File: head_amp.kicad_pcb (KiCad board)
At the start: 4 copper layers, 50 x 50 mm, 66 parts, among them J1 USB Interface, J2 Left_Speaker, J3 Left_Mic, J4 Right_Speaker, J5 Right_Mic, J6 AudioJack4, M1 Fan, Q1 LRC L8050QLT1G, Q2 LRC L8050QLT1G, SW1 Boot, SW2 Reset, U1 CH340K, U2 Digital Regulator, U3 Analog Regulator, U4 TXS0102DCU, U5 ESP32-S3-WROOM-1, U6 LSM6DS3, U7 WM8988LGECN/V, U8 WM8988LGECN/V

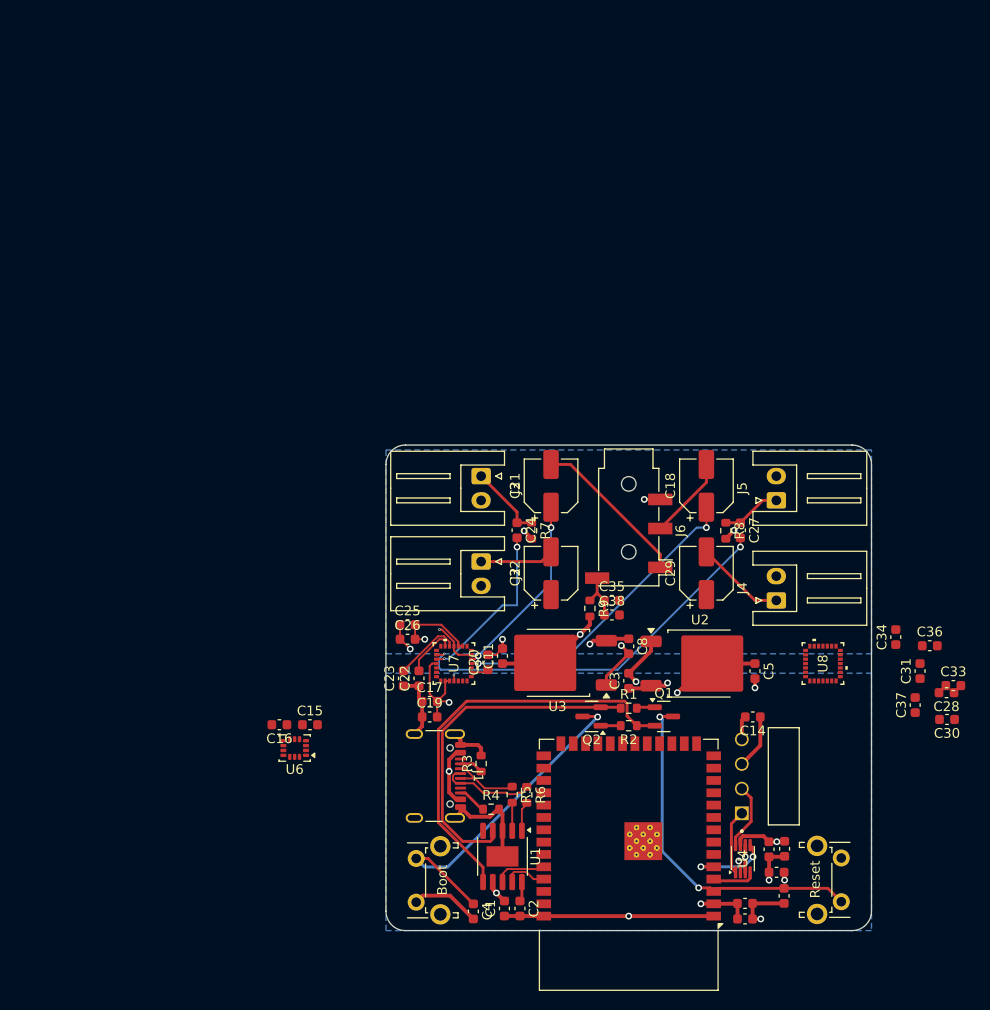
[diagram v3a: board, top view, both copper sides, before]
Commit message: feat: start hat version
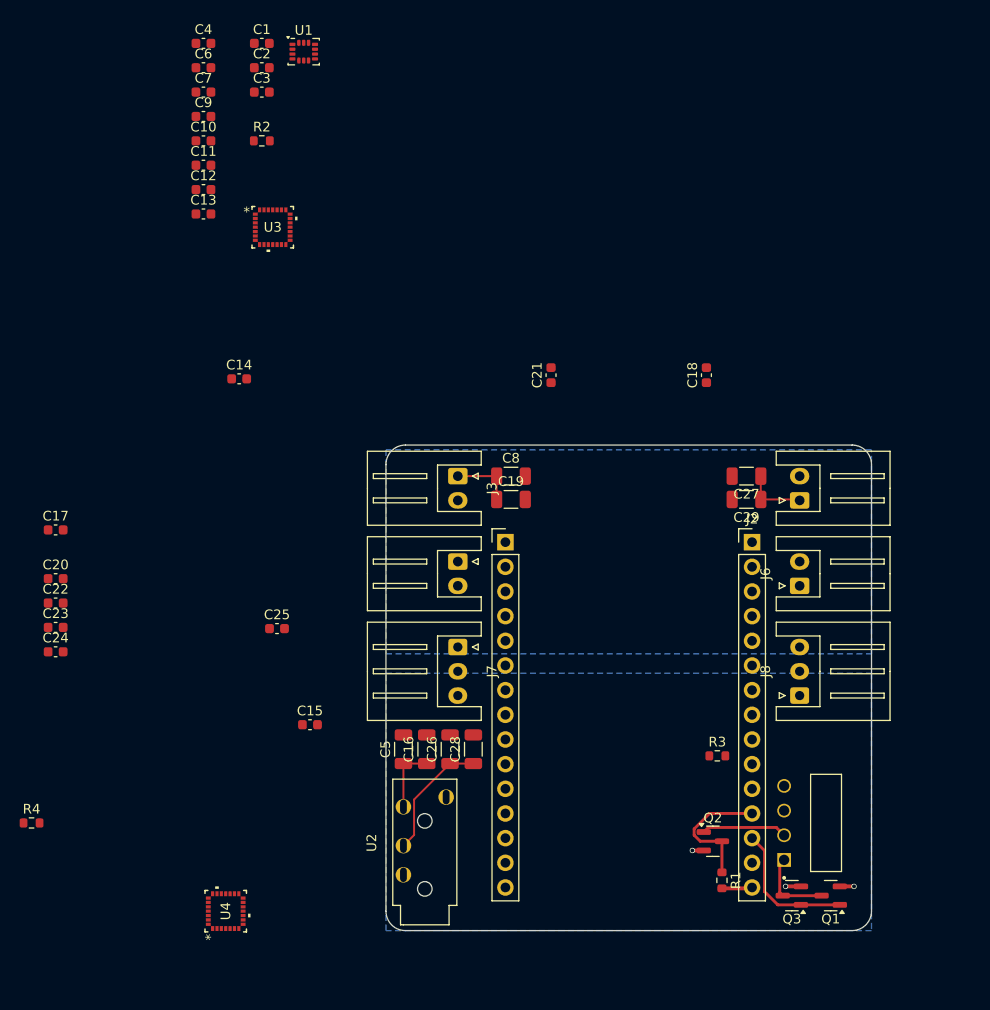
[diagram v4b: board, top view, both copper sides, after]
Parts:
- removed C30: 100n, Capacitor_SMD:C_0603_1608Metric
- removed C31, C33, C34, C36, C37: 4.7u, Capacitor_SMD:C_0603_1608Metric
- removed C32: 220u, Capacitor_SMD:CP_Elec_5x5.4
- removed C35, C38: 1u, Capacitor_SMD:C_0603_1608Metric
- removed R5, R6: 22, Resistor_SMD:R_0603_1608Metric
- removed R7, R8, R9: 10k, Resistor_SMD:R_0603_1608Metric
- removed SW1: Boot, Button_Switch_THT:SW_Tactile_SPST_Angled_PTS645Vx39-2LFS
- removed SW2: Reset, Button_Switch_THT:SW_Tactile_SPST_Angled_PTS645Vx39-2LFS
- removed U5: ESP32-S3-WROOM-1, RF_Module:ESP32-S3-WROOM-1
- removed U6: LSM6DS3, Package_LGA:LGA-14_3x2.5mm_P0.5mm_LayoutBorder3x4y
- removed U7, U8: WM8988LGECN/V, footprints:QFN28_4X4_CIR-M
- added J7: Conn_01x03, Connector_JST:JST_XH_S3B-XH-A_1x03_P2.50mm_Horizontal, F.Cu at (130.4, 96.8)
- added J8: Conn_01x03, Connector_JST:JST_XH_S3B-XH-A_1x03_P2.50mm_Horizontal, F.Cu at (165.6, 101.8)
- added Q3: AO3400A, Package_TO_SOT_SMD:SOT-23, F.Cu at (164.8, 122.4)
- C10, C12, C7: value 100n -> 4.7u
- C11: value 22u -> 1u
- C13, C24, C9: value 1u -> 4.7u
- C14: value 100n -> 1u
- C16, C19, C28: value 100n -> 100u; footprint Capacitor_SMD:C_0603_1608Metric -> Capacitor_SMD:C_1206_3216Metric
- C18, C21: value 220u -> 4.7u; footprint Capacitor_SMD:CP_Elec_5x5.4 -> Capacitor_SMD:C_0603_1608Metric
- C22, C25: value 4.7u -> 1u
- C26: value 4.7u -> 100u; footprint Capacitor_SMD:C_0603_1608Metric -> Capacitor_SMD:C_1206_3216Metric
- C27: value 1u -> 100u; footprint Capacitor_SMD:C_0603_1608Metric -> Capacitor_SMD:C_1206_3216Metric
- C29: value 220u -> 100u; footprint Capacitor_SMD:CP_Elec_5x5.4 -> Capacitor_SMD:C_1206_3216Metric
- C3: value 10u -> 100n
- C5: value 22u -> 100u; footprint Capacitor_SMD:C_0603_1608Metric -> Capacitor_SMD:C_1206_3216Metric
- C8: value 10u -> 100u; footprint Capacitor_SMD:C_0603_1608Metric -> Capacitor_SMD:C_1206_3216Metric
- J1: value USB Interface -> Conn_01x15; footprint Connector_USB:USB_C_Receptacle_GCT_USB4105-xx-A_16P_TopMnt_Horizontal -> Connector_PinHeader_2.54mm:PinHeader_1x15_P2.54mm_Vertical
- J2: value Left_Speaker -> Conn_01x15; footprint Connector_JST:JST_XH_S2B-XH-A_1x02_P2.50mm_Horizontal -> Connector_PinHeader_2.54mm:PinHeader_1x15_P2.54mm_Vertical
- J3: value Left_Mic -> Left_Speaker
- J4: value Right_Speaker -> Left_Mic
- J5: value Right_Mic -> Right_Speaker
- J6: value AudioJack4 -> Right_Mic; footprint Connector_Audio:Jack_3.5mm_PJ320D_Horizontal -> Connector_JST:JST_XH_S2B-XH-A_1x02_P2.50mm_Horizontal
- Q1: value LRC L8050QLT1G -> AO3401A
- Q2: value LRC L8050QLT1G -> AO3400A
- R3, R4: value 5.1k -> 10k
- U1: value CH340K -> LSM6DS3; footprint Package_SO:SSOP-10-1EP_3.9x4.9mm_P1mm_EP2.1x3.3mm -> Package_LGA:LGA-14_3x2.5mm_P0.5mm_LayoutBorder3x4y
- U2: value Digital Regulator -> PJ-320A; footprint Package_TO_SOT_SMD:TO-252-2 -> PJ-320A:PJ-320A
- U3: value Analog Regulator -> WM8988LGECN/V; footprint Package_TO_SOT_SMD:TO-252-2 -> footprints:QFN28_4X4_CIR-M
- U4: value TXS0102DCU -> WM8988LGECN/V; footprint Package_SO:VSSOP-8_2.3x2mm_P0.5mm -> footprints:QFN28_4X4_CIR-M
- moved C6 104.2 mm to (104.2, 37.1), turned to 0 degrees
- moved C7 99.7 mm to (104.2, 39.7)
- moved C9 98.4 mm to (104.2, 42.2), turned to 0 degrees
- moved C10 97.6 mm to (104.2, 44.7), turned to 0 degrees
- moved C4 93.6 mm to (104.2, 34.6), turned to 0 degrees
- moved C1 92.5 mm to (110.2, 34.6), turned to 0 degrees
- moved C2 90.6 mm to (110.2, 37.1), turned to 0 degrees
- moved C12 89.5 mm to (104.2, 49.7), turned to 0 degrees
- moved C13 88.6 mm to (104.2, 52.2), turned to 0 degrees
- moved U1 85.4 mm to (114.5, 35.5), turned to 0 degrees
- moved C3 71.4 mm to (110.2, 39.7), turned to 0 degrees
- moved R2 71.1 mm to (110.2, 44.7), turned to 0 degrees
- moved C14 63.3 mm to (107.9, 69.2), turned to 0 degrees
- moved C11 59.2 mm to (104.2, 47.2), turned to 0 degrees
- moved U3 53.6 mm to (111.3, 53.6), turned to 0 degrees
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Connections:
- C1 pad 1: GND -> +5V
- C1 pad 2: +3V3D -> GND
- C10 pad 2: +3V3D -> Net-(U3-VREF)
- C11 pad 1: +3V3A -> /Mic_Left
- C11 pad 2: GNDA -> Net-(U3-LINPUT1)
- C12 pad 1: GND -> GNDA
- C12 pad 2: VBUS -> +3V3A
- C13 pad 1: GND -> GNDA
- C13 pad 2: VBUS -> +3V3A
- C14 pad 1: VBUS -> /Mic_Right
- C14 pad 2: GND -> Net-(U3-RINPUT1)
- C15 pad 1: +3V3D -> GND
- C15 pad 2: GND -> +3V3D
- C16 pad 1: +3V3D -> /Headset_Left
- C16 pad 2: GND -> Net-(U3-LOUT1)
- C18 pad 1: Net-(U7-ROUT1) -> Net-(U4-HPCOM)
- C18 pad 2: /Headset_Right -> GNDA
- C19 pad 1: GND -> /Speaker_Left
- C19 pad 2: +3V3D -> Net-(U4-LOUT1)
- C2 pad 1: Net-(U1-V3) -> +3V3D
- C20 pad 1: Net-(U7-HPCOM) -> GND
- C20 pad 2: GNDA -> Net-(U4-VMID)
- C21 pad 1: Net-(U7-LOUT1) -> GND
- C21 pad 2: /Headset_Left -> Net-(U4-VREF)
- C22 pad 1: GND -> /Headset_Mic
- C22 pad 2: Net-(U7-VMID) -> Net-(U4-LINPUT1)
- C23 pad 1: GND -> GNDA
- C23 pad 2: Net-(U7-VREF) -> +3V3A
- C24 pad 1: /Mic_Left -> GNDA
- C24 pad 2: Net-(U7-LINPUT1) -> +3V3A
- C25 pad 1: GNDA -> /Headset_Mic
- C25 pad 2: +3V3A -> Net-(U4-RINPUT1)
- C26 pad 1: GNDA -> /Headset_Right
- C26 pad 2: +3V3A -> Net-(U3-ROUT1)
- C27 pad 1: /Mic_Right -> /Speaker_Right
- C27 pad 2: Net-(U7-RINPUT1) -> Net-(U4-ROUT1)
- C28 pad 1: GND -> /Headset_Right
- C28 pad 2: +3V3D -> Net-(U3-ROUT1)
- C29 pad 1: Net-(U8-ROUT1) -> /Speaker_Right
- C29 pad 2: /Speaker_Right -> Net-(U4-ROUT1)
- C3 pad 1: VBUS -> +3V3D
- C4 pad 1: /GPIO0 -> GND
- C4 pad 2: GND -> +3V3D
- C5 pad 1: +3V3D -> /Headset_Left
- C5 pad 2: GND -> Net-(U3-LOUT1)
- C6 pad 1: /MCU_EN -> GND
- C6 pad 2: GND -> +3V3D
- C7 pad 1: GND -> Net-(U3-HPCOM)
- C7 pad 2: +3V3D -> GNDA
- C8 pad 1: VBUS -> /Speaker_Left
- C8 pad 2: GNDA -> Net-(U4-LOUT1)
- C9 pad 2: +3V3D -> Net-(U3-VMID)
- J2 pad 1: /Speaker_Left -> unconnected-(J2-Pin_1-Pad1)
- J2 pad 2: GNDA -> unconnected-(J2-Pin_2-Pad2)
- J3 pad 1: /Mic_Left -> /Speaker_Left
- J4 pad 1: /Speaker_Right -> /Mic_Left
- J5 pad 1: /Mic_Right -> /Speaker_Right
- M1 pad 2: VBUS -> +5V
- Q1 pad 1: Net-(Q1-B) -> /FAN_PWM
- Q1 pad 2: /RTS -> +5V
- Q1 pad 3: /MCU_EN -> Net-(M1-PWM)
- Q2 pad 1: Net-(Q2-B) -> Net-(M1-Tacho)
- Q2 pad 2: /DTR -> GND
- Q2 pad 3: /GPIO0 -> /FAN_RPM
- R1 pad 1: /DTR -> /FAN_RPM
- R1 pad 2: Net-(Q1-B) -> +3V3D
- R2 pad 1: /RTS -> /Mic_Left
- R2 pad 2: Net-(Q2-B) -> +3V3A
- R3 pad 1: Net-(J1-CC1) -> /Mic_Right
- R3 pad 2: GND -> +3V3A
- R4 pad 1: Net-(J1-CC2) -> +3V3A
- R4 pad 2: GND -> /Headset_Mic
- U1 pad 1: /USB_D+ -> /MISO
- U1 pad 10: Net-(U1-V3) -> unconnected-(U1-NC-Pad10)
- U1 pad 11: GND -> unconnected-(U1-NC-Pad11)
- U1 pad 2: /USB_D- -> GND
- U1 pad 4: /DTR -> unconnected-(U1-INT1-Pad4)
- U1 pad 5: unconnected-(U1-~{CTS}-Pad5) -> +3V3D
- U1 pad 6: /RTS -> GND
- U1 pad 7: +3V3D -> GND
- U1 pad 8: /MCU_RX -> +3V3D
- U1 pad 9: /MCU_TX -> unconnected-(U1-INT2-Pad9)
- U2 pad 1: GND -> /Headset_Mic
- U2 pad 2: +3V3D -> /Headset_Left
- U2 pad 3: VBUS -> /Headset_Right
- U3 pad 1: GNDA -> /Ext->Int/Master_CLK
- U3 pad 2: +3V3A -> +3V3D
- U3 pad 3: VBUS -> +3V3D
- U4 pad 1: Net-(M1-PWM) -> /Int->Ext/Master_CLK
- U4 pad 2: GND -> +3V3D
- U4 pad 4: /FAN_PWM -> GND
- U4 pad 5: /FAN_RPM -> /Int->Ext_CLK
- U4 pad 6: +3V3D -> /Int->Ext_In
- U4 pad 7: VBUS -> /Int->Ext_LRC
- U4 pad 8: Net-(M1-Tacho) -> /Int->Ext_Out
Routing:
- net GND: track 72.5 -> 2.76 mm, vias 7 -> 2
- net /RTS: track 42.9 -> 0.00 mm
- net Net-(U7-RINPUT1): track 39.8 -> 0.00 mm, vias 2 -> 0
- net /MCU_EN: track 36.2 -> 0.00 mm, vias 2 -> 0
- net /DTR: track 35.7 -> 0.00 mm
- net /GPIO0: track 34.9 -> 0.00 mm, vias 1 -> 0
- net Net-(U7-ROUT1): track 32.1 -> 0.00 mm, vias 2 -> 0
- net +3V3D: track 31.2 -> 3.14 mm, vias 6 -> 0
- net VBUS: track 26.0 -> 0.00 mm, vias 4 -> 0
- net +3V3A: track 22.5 -> 0.00 mm, vias 4 -> 0
- net Net-(U7-LOUT1): track 19.3 -> 0.00 mm, vias 2 -> 0
- net GNDA: track 17.6 -> 0.00 mm, vias 5 -> 0
- net Net-(U7-LINPUT1): track 17.5 -> 0.00 mm, vias 2 -> 0
- net /FAN_PWM: track 4.55 -> 14.4 mm
- net /USB_D1+: track 9.79 -> 0.00 mm
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- added copper zone on In1.Cu, net +5V
- removed copper zone on In1.Cu, net VBUS

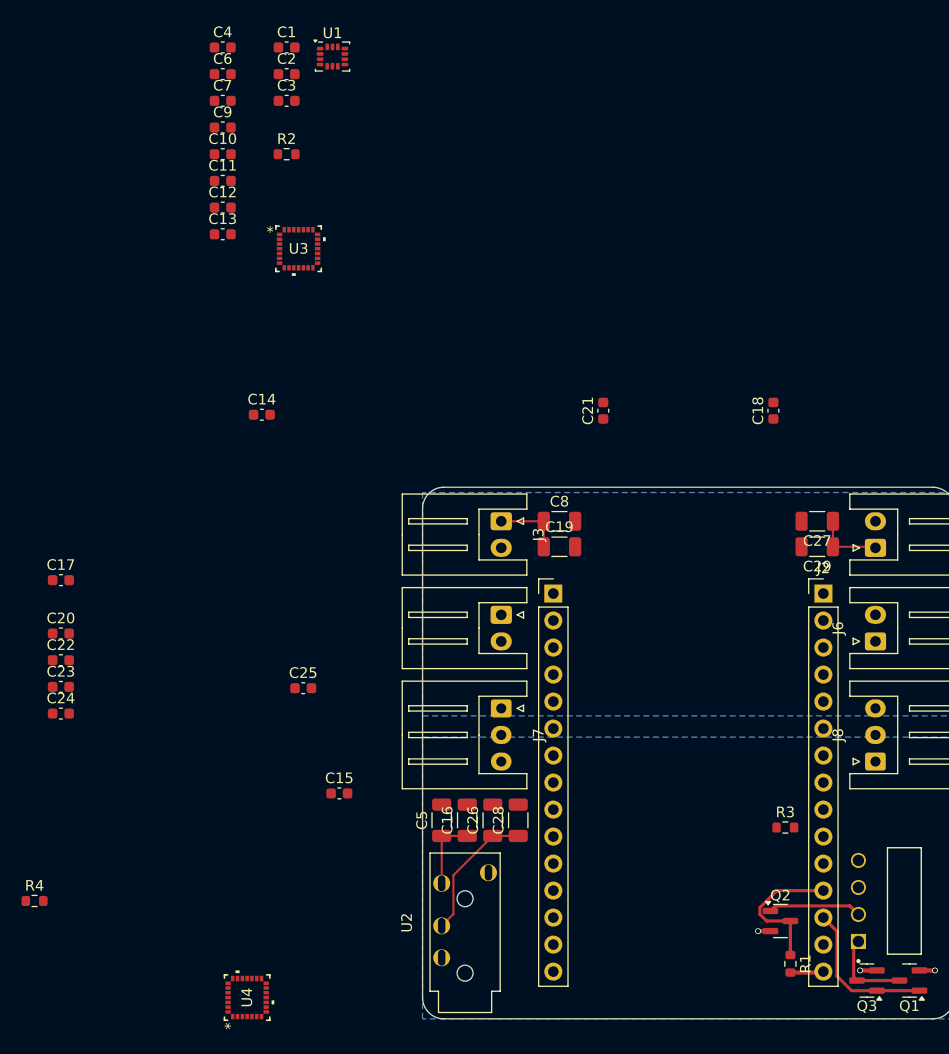
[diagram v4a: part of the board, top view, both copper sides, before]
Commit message: More capacitor layed
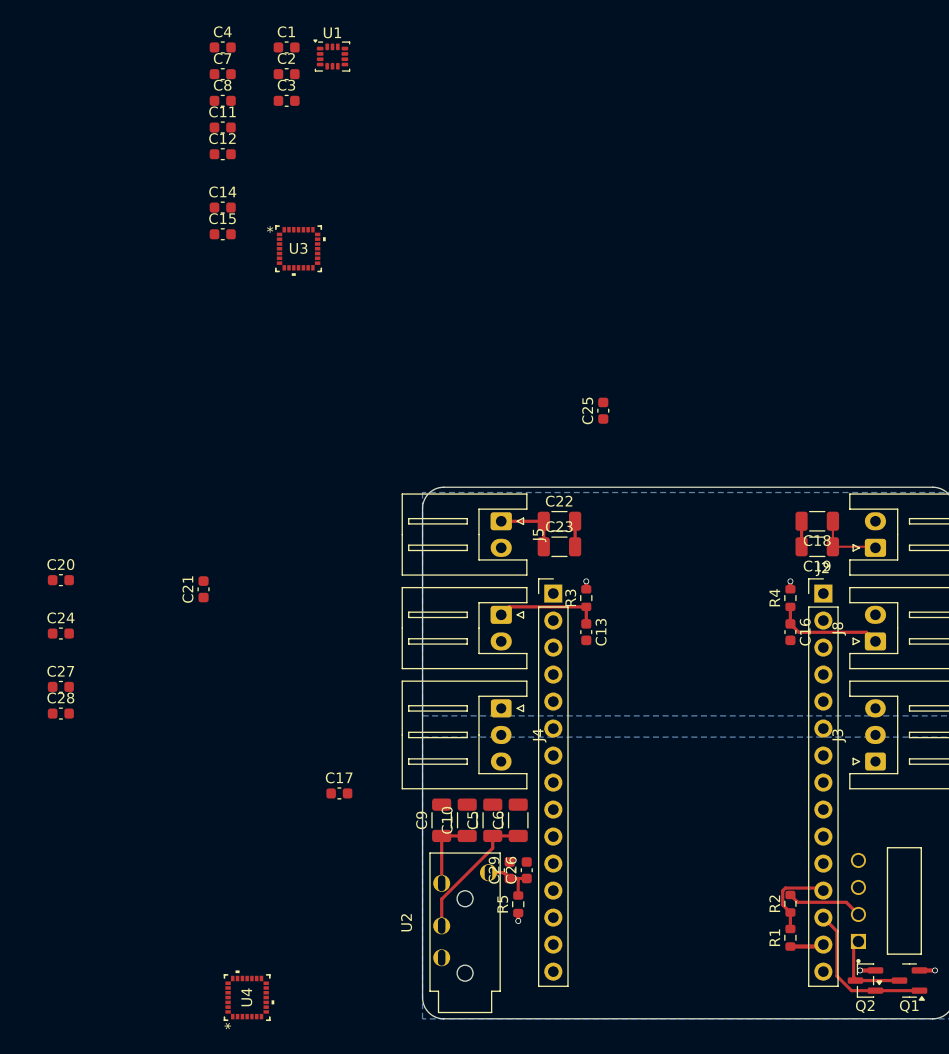
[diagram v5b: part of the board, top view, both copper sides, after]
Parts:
- removed Q3: AO3400A, Package_TO_SOT_SMD:SOT-23
- added R2: 27k, Resistor_SMD:R_0603_1608Metric, F.Cu at (157.6, 115.2)
- R1: value 10k -> 50k
- moved C21 56.2 mm to (102.4, 85.6)
- moved C13 54.5 mm to (138.4, 89.6), turned to -90 degrees
- moved C16 53.8 mm to (157.6, 89.6), turned to -90 degrees
- moved R3 50.4 mm to (138.4, 86.4), turned to 90 degrees
- moved C26 48.1 mm to (132.8, 112.0), turned to 90 degrees
- moved R5 45.5 mm to (132.0, 115.2), turned to 90 degrees
- moved C29 25.9 mm to (131.2, 112.0), turned to 90 degrees
- moved R4 21.6 mm to (157.6, 86.4), turned to 90 degrees
- moved Q2 9.77 mm to (164.7, 122.4), turned to 180 degrees
- moved R1 2.45 mm to (157.6, 118.4), turned to 90 degrees
- renumbered C16 to C10, C9 to C11, C10 to C12, C11 to C13, C12 to C14, C13 to C15, C14 to C16, C15 to C17, C27 to C18, C29 to C19, C17 to C20, C18 to C21, C8 to C22, C19 to C23, C20 to C24, C21 to C25, C22 to C26, C23 to C27, C24 to C28, C25 to C29, C26 to C5, C28 to C6, C6 to C7, C7 to C8, C5 to C9, J8 to J3, J7 to J4, J3 to J5, J4 to J6, J5 to J7, J6 to J8, R2 to R3, R3 to R4, R4 to R5
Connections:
- Q2 pad 1: Net-(M1-Tacho) -> /FAN_PWM
- Q2 pad 3: /FAN_RPM -> Net-(M1-PWM)
- R1 pad 1: /FAN_RPM -> GND
- R1 pad 2: +3V3D -> /FAN_RPM
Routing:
- net /Mic_Right: track 0.00 -> 10.3 mm
- net /Mic_Left: track 0.00 -> 9.91 mm
- net /FAN_RPM: track 13.6 -> 7.93 mm
- net /Headset_Mic: track 0.00 -> 5.43 mm
- net +3V3D: track 3.14 -> 0.13 mm
- net Net-(U4-ROUT1): track 0.00 -> 2.40 mm
- net Net-(U4-LOUT1): track 0.00 -> 2.40 mm
- net +3V3A: track 0.00 -> 2.25 mm, vias 0 -> 3
- net GND: track 2.76 -> 4.76 mm, vias 2 -> 1
- net Net-(M1-Tacho): track 8.80 -> 7.16 mm

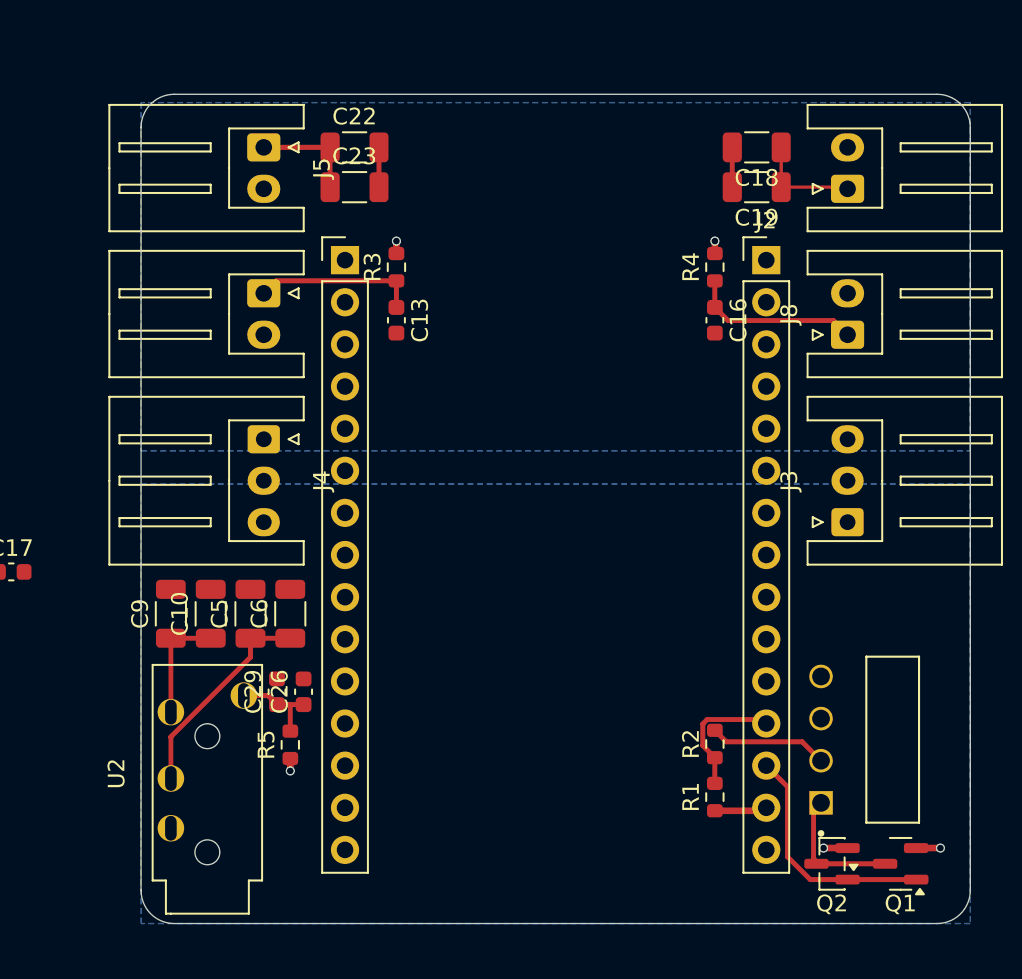
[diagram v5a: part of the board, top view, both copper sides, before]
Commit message: Remove conflict silkscreen
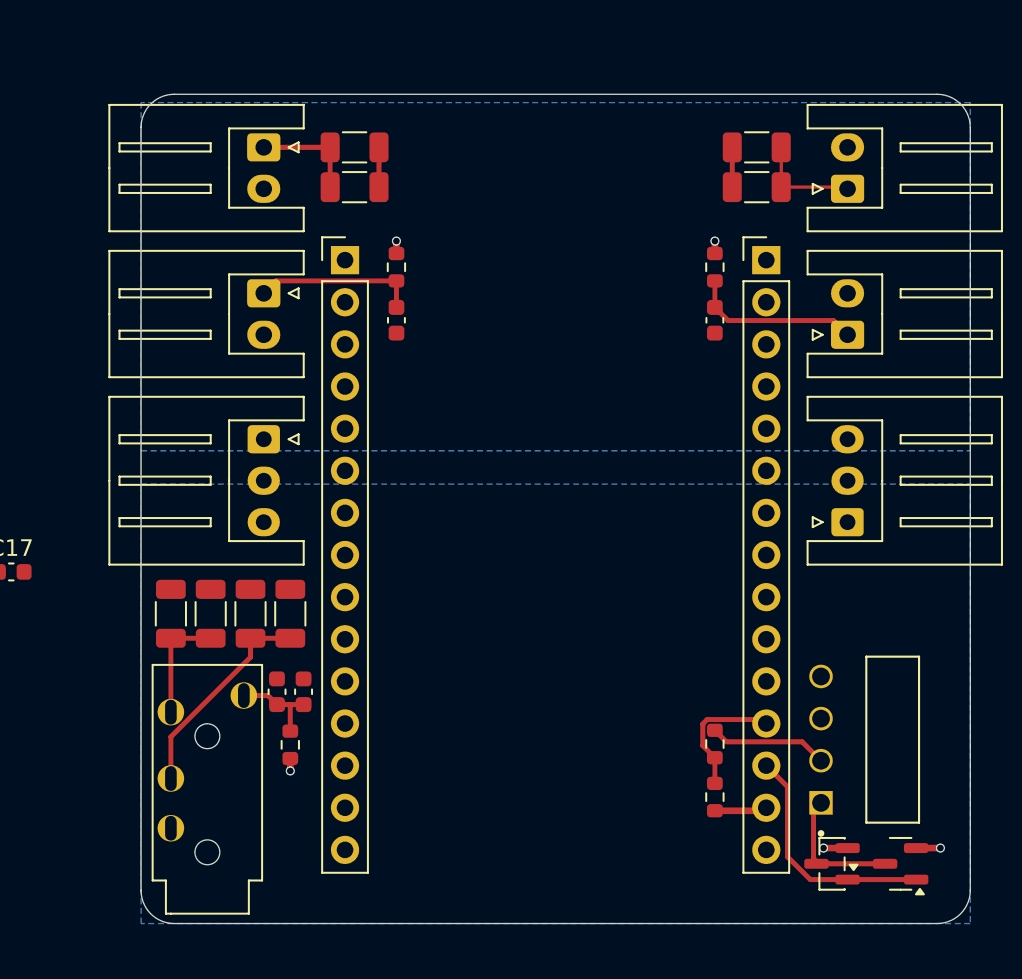
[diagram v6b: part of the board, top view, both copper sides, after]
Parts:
- U2: value PJ-320A -> Headphone Jack
